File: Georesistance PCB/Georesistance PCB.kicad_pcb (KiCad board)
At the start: 4 copper layers, 87 parts, among them J1 Screw_Terminal_01x04, J2 Screw_Terminal_01x02, J3 Conn_01x11_Male, Q1 MMBF4117, Q2 MMBF4117, Q3 MMBF4117, Q4 MMBF4117, Q5 SI3430DV, Q6 SI3430DV, Q7 LNC045R090, Q8 TIP122, U1 RS8554, U10 LM350_TO220, U2 LTC6915HGN-TRPBF, U3 LM4040DBZ-2.5, U4 RS8552, U5 TXS0108EPWR, U6 ADS1115IDGS, U7 LM2776, U8 LM337L_TO92, U9 AP2127N-2.5

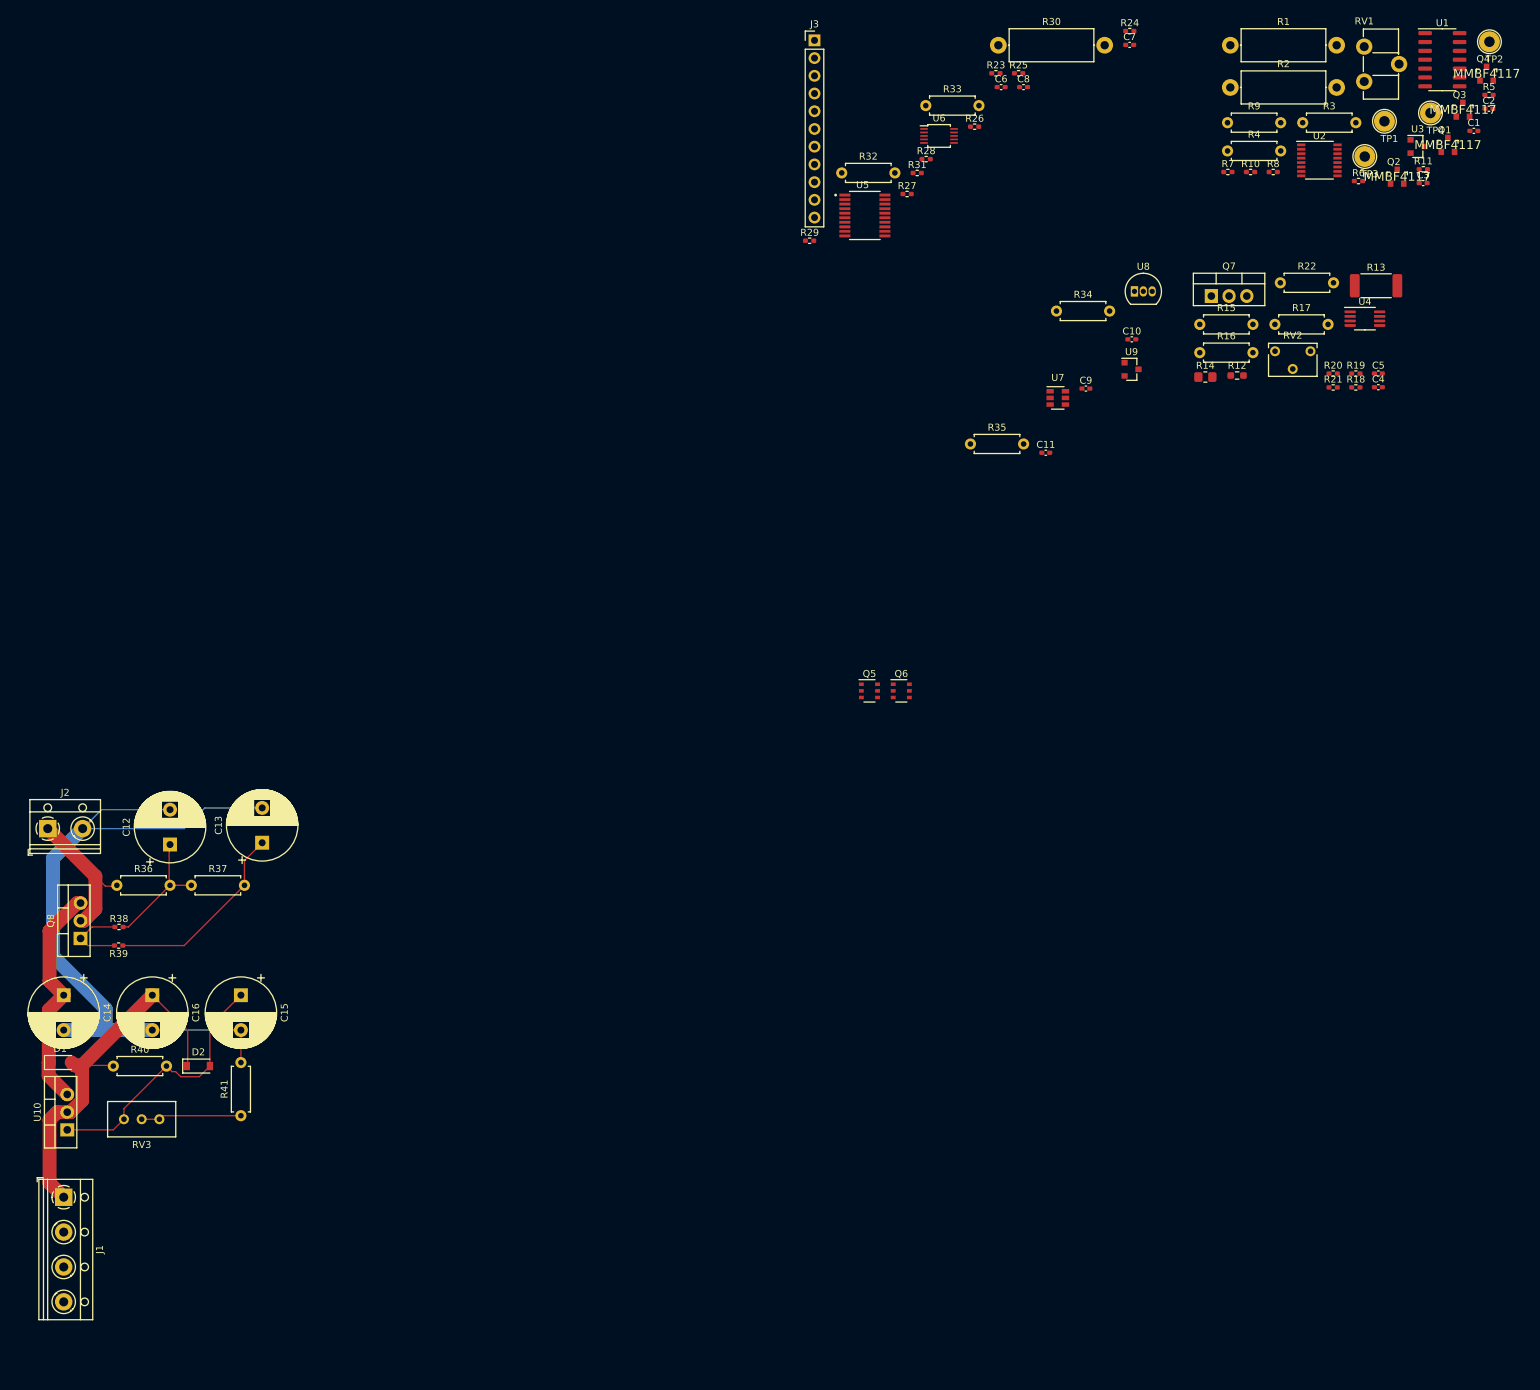
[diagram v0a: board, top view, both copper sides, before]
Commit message: Added the PCB layout and simplified schematic
deleted jumper, and fixed misconnection
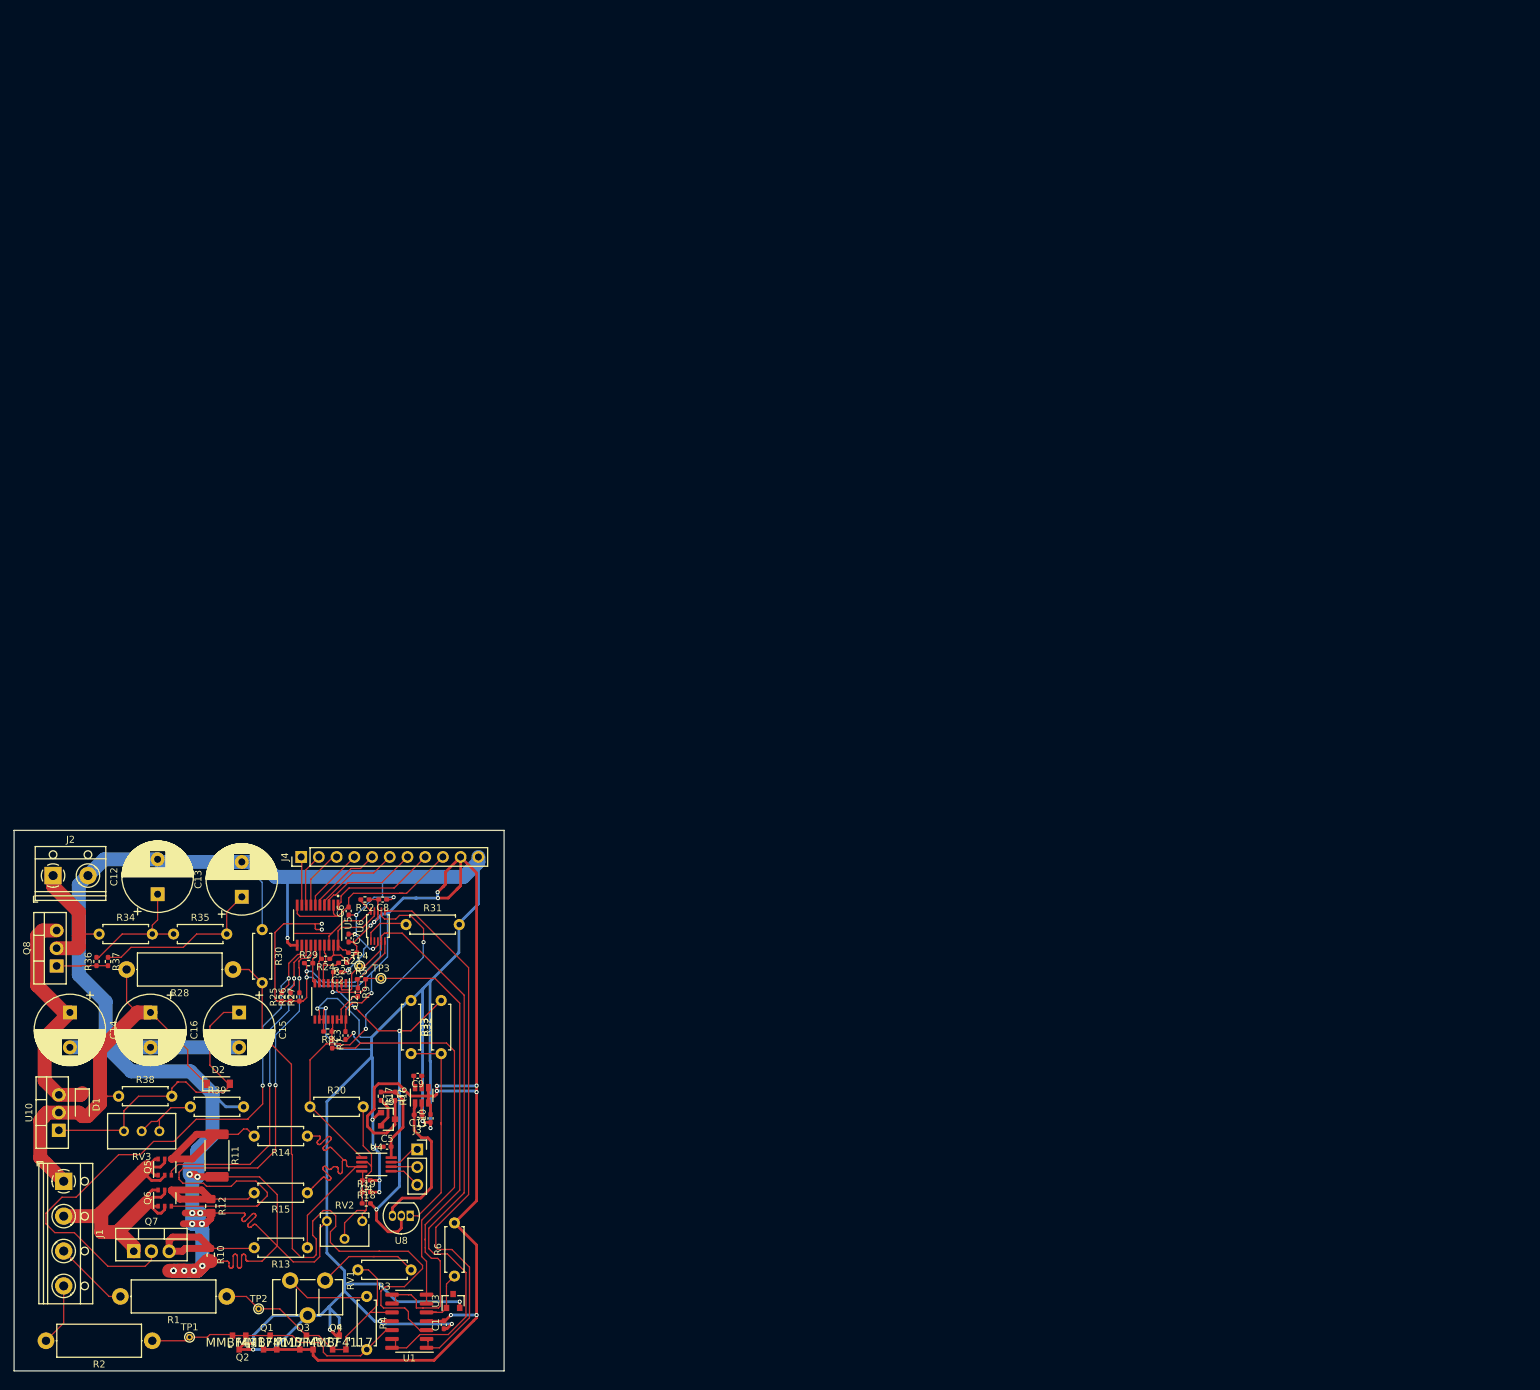
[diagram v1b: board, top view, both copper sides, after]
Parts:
- removed the R30 at (153.8, -93.5)
- removed the R31 at (142.1, -75.2)
- removed the R34 at (162.1, -55.4)
- removed the R35 at (149.8, -36.3)
- removed R41: 10k, Resistor_THT:R_Axial_DIN0207_L6.3mm_D2.5mm_P7.62mm_Horizontal
- added J4: Conn_01x11_Male, Connector_PinHeader_2.54mm:PinHeader_1x11_P2.54mm_Vertical, F.Cu at (53.8, 22.9)
- added R32: 180, Resistor_THT:R_Axial_DIN0207_L6.3mm_D2.5mm_P7.62mm_Horizontal, F.Cu at (69.6, 43.4)
- added R33: 180, Resistor_THT:R_Axial_DIN0207_L6.3mm_D2.5mm_P7.62mm_Horizontal, F.Cu at (73.9, 51.1)
- added R39: 10k, Resistor_THT:R_Axial_DIN0207_L6.3mm_D2.5mm_P7.62mm_Horizontal, F.Cu at (38.0, 58.7)
- J3: value Conn_01x11_Male -> Conn_01x03_Male; footprint Connector_PinHeader_2.54mm:PinHeader_1x11_P2.54mm_Vertical -> Connector_PinSocket_2.54mm:PinSocket_1x03_P2.54mm_Vertical
- R10: value 0 -> 25m; footprint Resistor_SMD:R_0402_1005Metric_Pad0.72x0.64mm_HandSolder -> Resistor_SMD:R_0603_1608Metric_Pad0.98x0.95mm_HandSolder
- R11: value 0 -> 400m; footprint Resistor_SMD:R_0402_1005Metric_Pad0.72x0.64mm_HandSolder -> Resistor_SMD:R_2512_6332Metric_Pad1.40x3.35mm_HandSolder
- R12: value 25m -> 6.2; footprint Resistor_SMD:R_0603_1608Metric_Pad0.98x0.95mm_HandSolder -> Resistor_SMD:R_0805_2012Metric_Pad1.20x1.40mm_HandSolder
- R13: value 400m -> 10M; footprint Resistor_SMD:R_2512_6332Metric_Pad1.40x3.35mm_HandSolder -> Resistor_THT:R_Axial_DIN0207_L6.3mm_D2.5mm_P7.62mm_Horizontal
- R14: value 6.2 -> 10M; footprint Resistor_SMD:R_0805_2012Metric_Pad1.20x1.40mm_HandSolder -> Resistor_THT:R_Axial_DIN0207_L6.3mm_D2.5mm_P7.62mm_Horizontal
- R16, R17: value 10M -> 0; footprint Resistor_THT:R_Axial_DIN0207_L6.3mm_D2.5mm_P7.62mm_Horizontal -> Resistor_SMD:R_0402_1005Metric_Pad0.72x0.64mm_HandSolder
- R20: value 0 -> 1k; footprint Resistor_SMD:R_0402_1005Metric_Pad0.72x0.64mm_HandSolder -> Resistor_THT:R_Axial_DIN0207_L6.3mm_D2.5mm_P7.62mm_Horizontal
- R21: value 0 -> DNP
- R22: value 1k -> DNP; footprint Resistor_THT:R_Axial_DIN0207_L6.3mm_D2.5mm_P7.62mm_Horizontal -> Resistor_SMD:R_0402_1005Metric_Pad0.72x0.64mm_HandSolder
- R28: value DNP -> 200M; footprint Resistor_SMD:R_0402_1005Metric_Pad0.72x0.64mm_HandSolder -> Resistor_THT:R_Axial_DIN0414_L11.9mm_D4.5mm_P15.24mm_Horizontal
- R6: value 0 -> 10k; footprint Resistor_SMD:R_0402_1005Metric_Pad0.72x0.64mm_HandSolder -> Resistor_THT:R_Axial_DIN0207_L6.3mm_D2.5mm_P7.62mm_Horizontal
- R9: value 10k -> 0; footprint Resistor_THT:R_Axial_DIN0207_L6.3mm_D2.5mm_P7.62mm_Horizontal -> Resistor_SMD:R_0402_1005Metric_Pad0.72x0.64mm_HandSolder
- TP1, TP2, TP3, TP4: footprint TestPoint:TestPoint_Loop_D2.54mm_Drill1.5mm_Beaded -> TestPoint:TestPoint_THTPad_D1.0mm_Drill0.5mm
- moved TP2 253.2 mm to (47.8, 87.6)
- moved Q4 245.2 mm to (59.3, 92.5)
- moved TP1 244.4 mm to (37.8, 91.7)
- moved Q3 242.3 mm to (54.6, 92.5)
- moved Q1 240.8 mm to (49.4, 92.5)
- moved R2 237.0 mm to (32.5, 92.2), turned to 180 degrees
- moved Q2 235.5 mm to (45.0, 92.5), turned to 180 degrees
- moved U1 233.7 mm to (69.3, 89.4), turned to 180 degrees
- moved RV1 231.2 mm to (57.3, 83.6), turned to 270 degrees
- moved R1 229.9 mm to (43.2, 85.9), turned to 180 degrees
- moved C1 226.0 mm to (74.3, 89.9), turned to 90 degrees
- moved R11 223.3 mm to (41.8, 65.7), turned to 270 degrees
- moved U3 215.6 mm to (75.6, 86.5), turned to 90 degrees
- moved R10 215.2 mm to (40.9, 79.9), turned to 270 degrees
- moved R3 208.3 mm to (69.6, 82.0), turned to 180 degrees
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- renumbered R32 to R30, R33 to R31, R36 to R34, R37 to R35, R38 to R36, R39 to R37, R40 to R38
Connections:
- J3 pad 1: GND -> OP_O
- J3 pad 2: LVL_C -> OP_N
- J3 pad 3: LVL_B -> OP_P
- R1 pad 2: Pasak_A -> Pasak_M
- R10 pad 1: /Voltage_Sense/Ref_Selector -> /Current_Sense/R_A
- R10 pad 2: 2.5V_Ref -> GND
- R11 pad 1: /Voltage_Sense/Ref_Selector -> /Current_Sense/R_B
- R12 pad 1: /Current_Sense/R_A -> /Current_Sense/R_C
- R13 pad 1: /Current_Sense/R_B -> Net-(R13-Pad1)
- R13 pad 2: GND -> /Current_Sense/R_A
- R14 pad 1: /Current_Sense/R_C -> Net-(R13-Pad1)
- R14 pad 2: GND -> /Current_Sense/R_B
- R15 pad 1: Net-(R15-Pad1) -> Net-(R13-Pad1)
- R15 pad 2: /Current_Sense/R_A -> /Current_Sense/R_C
- R16 pad 1: Net-(R15-Pad1) -> Net-(C5-Pad2)
- R16 pad 2: /Current_Sense/R_B -> +5V
- R17 pad 1: Net-(R15-Pad1) -> Net-(C5-Pad2)
- R17 pad 2: /Current_Sense/R_C -> +2V5
- R18 pad 1: Net-(C5-Pad2) -> Net-(C4-Pad2)
- R18 pad 2: +5V -> -2V5
- R19 pad 1: Net-(C5-Pad2) -> Net-(C4-Pad2)
- R19 pad 2: +2V5 -> GND
- R2 pad 2: Pasak_B -> Pasak_N
- R20 pad 1: Net-(C4-Pad2) -> ADC_3
- R20 pad 2: -2V5 -> Net-(R20-Pad2)
- R21 pad 1: Net-(C4-Pad2) -> +5V
- R21 pad 2: GND -> SDA_5V
- R22 pad 1: ADC_2 -> +5V
- R22 pad 2: Net-(R22-Pad2) -> SCL_5V
- R23 pad 1: Net-(R23-Pad1) -> +5V
- R23 pad 2: SDA_5V -> CS_5V
- R24 pad 1: Net-(R23-Pad1) -> +5V
- R24 pad 2: SCL_5V -> MOSI_5V
- R25 pad 1: Net-(R23-Pad1) -> +5V
- R25 pad 2: CS_5V -> LVL_A_5V
- R26 pad 1: Net-(R23-Pad1) -> +5V
- R26 pad 2: MOSI_5V -> LVL_B_5V
- R28 pad 1: +5V -> Net-(R28-Pad1)
- R28 pad 2: LVL_B_5V -> Pasak_A
- R29 pad 2: LVL_A_5V -> CLK_5V
- R30 pad 2: Net-(R30-Pad1) -> Net-(R28-Pad1)
- R5 pad 1: ADC_0 -> ADC_1
- R5 pad 2: Net-(Q3-Pad3) -> Net-(R5-Pad2)
- R6 pad 2: Net-(Q3-Pad3) -> +5V
- R7 pad 1: Net-(R7-Pad1) -> /Voltage_Sense/Ref_Selector
- R7 pad 2: Net-(Q1-Pad3) -> 2.5V_Ref
- R8 pad 1: ADC_1 -> /Voltage_Sense/Ref_Selector
- R8 pad 2: Net-(Q1-Pad3) -> GND
- R9 pad 1: Net-(R9-Pad1) -> ADC_1
- R9 pad 2: +5V -> Net-(R9-Pad2)
- RV2 pad 1: Net-(R22-Pad2) -> Net-(R20-Pad2)
- RV2 pad 2: Net-(R22-Pad2) -> Net-(R20-Pad2)
- TP3 pad 1: Net-(Q3-Pad3) -> Net-(R5-Pad2)
- TP4 pad 1: Net-(Q1-Pad3) -> ADC_0
- U1 pad 1: Net-(Q3-Pad3) -> ADC_2
- U1 pad 10: Net-(R30-Pad1) -> Net-(Q3-Pad3)
- U1 pad 12: Net-(R9-Pad1) -> Net-(Q1-Pad3)
- U1 pad 13: 2.5V_Ref -> ADC_0
- U1 pad 14: 2.5V_Ref -> ADC_0
- U1 pad 2: Net-(Q3-Pad3) -> ADC_2
- U1 pad 3: Net-(Q3-Pad3) -> Net-(R28-Pad1)
- U1 pad 5: Net-(Q1-Pad3) -> Net-(R6-Pad1)
- U1 pad 6: Net-(Q1-Pad3) -> 2.5V_Ref
- U1 pad 7: Net-(Q1-Pad3) -> 2.5V_Ref
- U1 pad 8: ADC_3 -> Net-(R5-Pad2)
- U1 pad 9: ADC_3 -> Net-(R5-Pad2)
- U2 pad 1: Net-(U2-Pad1) -> (no net)
- U2 pad 12: Net-(U2-Pad12) -> (no net)
- U2 pad 14: Out -> Net-(R9-Pad2)
- U2 pad 15: Out -> Net-(R9-Pad2)
- U2 pad 2: Net-(R7-Pad1) -> ADC_0
- U2 pad 3: Net-(R6-Pad1) -> Net-(R5-Pad2)
- U2 pad 5: Net-(U2-Pad5) -> (no net)
- U2 pad 9: Net-(U2-Pad9) -> (no net)
- U3 pad 1: Net-(R9-Pad1) -> Net-(R6-Pad1)
- U4 pad 1: ADC_2 -> ADC_3
- U4 pad 2: Net-(R22-Pad2) -> Net-(R20-Pad2)
- U4 pad 3: Net-(R15-Pad1) -> Net-(R13-Pad1)
- U4 pad 5: (no net) -> OP_P
- U4 pad 6: (no net) -> OP_N
- U4 pad 7: (no net) -> OP_O
- U5 pad 12: LVL_C_5V -> LVL_A_5V
- U5 pad 14: LVL_A_5V -> LVL_C_5V
- U5 pad 7: LVL_A -> LVL_C
- U5 pad 9: LVL_C -> LVL_A
- U6 pad 2: Net-(U6-Pad2) -> (no net)
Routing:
- net GND: track 104.4 -> 564.3 mm, vias 0 -> 33
- net +5V: track 0.00 -> 279.1 mm, vias 0 -> 15
- net Net-(R28-Pad1): track 0.00 -> 96.3 mm
- net ADC_0: track 0.00 -> 93.0 mm
- net LVL_A_5V: track 0.00 -> 87.1 mm, vias 0 -> 2
- net ADC_2: track 0.00 -> 80.4 mm
- net LVL_C_5V: track 0.00 -> 79.6 mm, vias 0 -> 2
- net Net-(R5-Pad2): track 0.00 -> 78.3 mm
- net -2V5: track 0.00 -> 59.5 mm, vias 0 -> 4
- net 2.5V_Ref: track 0.00 -> 56.7 mm
- net Pasak_B: track 0.00 -> 53.6 mm
- net ADC_3: track 0.00 -> 52.8 mm, vias 0 -> 2
- net LVL_B_5V: track 0.00 -> 49.7 mm, vias 0 -> 2
- net Net-(R13-Pad1): track 0.00 -> 42.9 mm
- net Net-(Q1-Pad3): track 0.00 -> 40.1 mm
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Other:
- board outline added: 70.2 x 77.5 mm

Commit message: added things
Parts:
- added H1: MountingHole, MountingHole:MountingHole_3.2mm_M3_DIN965, F.Cu at (20.1, 93.1)
- added H2: MountingHole, MountingHole:MountingHole_3.2mm_M3_DIN965, F.Cu at (93.2, 93.1)
- added H3: MountingHole, MountingHole:MountingHole_3.2mm_M3_DIN965, F.Cu at (20.1, 25.3)
- added H4: MountingHole, MountingHole:MountingHole_3.2mm_M3_DIN965, F.Cu at (93.2, 25.3)
- moved J2 8.50 mm to (26.7, 26.9)
- moved C11 8.37 mm to (78.9, 61.2)
- moved C8 8.37 mm to (73.8, 30.4)
- moved C9 8.37 mm to (78.8, 55.6)
- moved U6 8.37 mm to (73.1, 34.2)
- moved U9 8.37 mm to (74.5, 61.8)
- moved U8 8.37 mm to (77.7, 75.7)
- moved C12 8.37 mm to (41.5, 29.6)
- moved C13 8.37 mm to (53.6, 30.0)
- moved C15 8.37 mm to (53.2, 46.5)
- moved C2 8.37 mm to (67.3, 40.8)
- moved C3 8.37 mm to (68.5, 49.9)
- moved C6 8.37 mm to (68.9, 32.0)
- moved D1 8.37 mm to (30.7, 59.8)
- moved J4 8.37 mm to (62.1, 24.3)
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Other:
- board size 70.2 x 77.5 mm -> 82.3 x 76.8 mm
- board text added: "25m"
- board text added: "3V3"
- board text added: "400m"
- board text added: "5V"
- board text added: "6.2"
- board text added: "A"
- board text added: "B"
- board text added: "C"
- board text added: "CLK"
- board text added: "CS"
- board text added: "D"
- board text added: "GND"
- board text added: "MOSI"
- board text added: "Op Amp Supply Config V+: R16 for 5V supply R17 for 2.5V supply V-: R18 for -2.5V R19 for GND"
- board text added: "Possible Configuration in this board"
- board text added: "R16 for 5V supply R17 for 2.5V supply"
- board text added: "R18 for -2.5V R19 for GND"
- board text added: "R5 for direct connection R9 for inst. amp output"
- board text added: "R7 for 2.5 Ref R8 for GND Ref"
- board text added: "SCL"
- board text added: "SDA"
- board text added: "V Sense config: R5 for direct connection R9 for inst. amp output Inst. Amp. Ref config: R7 for 2.5 Ref R8 for GND Ref"
- board text added: "VCC"
